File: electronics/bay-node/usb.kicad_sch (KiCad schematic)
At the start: 21 parts, among them J3 PC, J4 DUT, J7 DATA, SW3 SERVICE, U4 USBLC6-2SC6, U5 MUX_PC, U6 MUX_DUT, U7 SN74LVC1G32DBVR, U8 USBLC6-2SC6

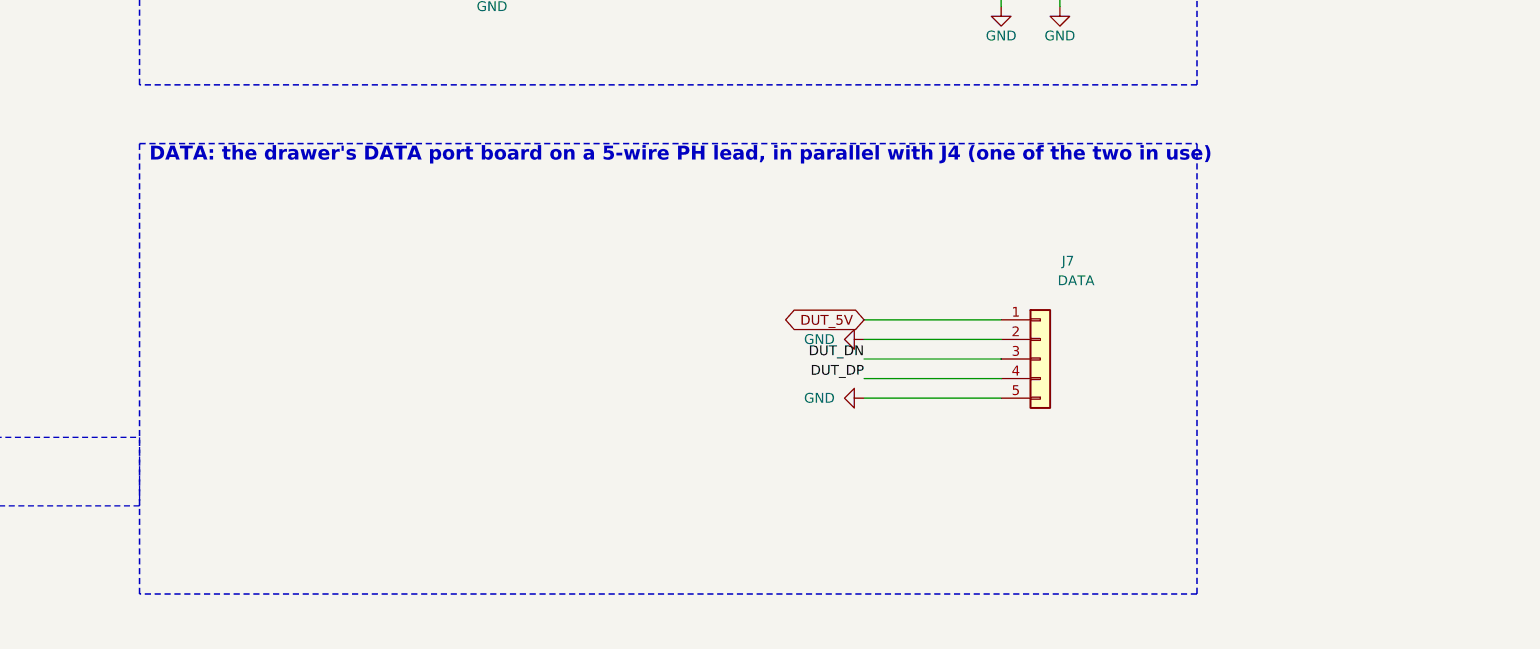
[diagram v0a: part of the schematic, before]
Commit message: DATA lead on 8 wires: node J7 a vertical PH 8 (USB, I²C, INT), data port J2 an S8B
Density decisions of 2026-10-19: the DATA lead becomes the camera's PH 8
"Same direction" type and also carries the node's I²C and an open-drain,
active-low INT (IO4, 10k pull-up, 1k at J7) for a later DATA ×4 board.

- Node: J7 B8B vertical by the right edge (J5's old slot), J5 AUX
  horizontal in the middle, AUX parts in a column between them.  J7 now
  taps the pair at J4's pads (DUT_CONN_*, behind U8's ESD like J4); the
  branch is hand-drawn in usb_hs_routes() on B.Cu under J4, since
  Freerouting found no room on U8's mux side.  ERC 0, DRC 0, parity 0,
  99 models.
- Data port: S8B, pins 1–3 open, PH at x 14.4, left hole (2.6, 13.5),
  one silkscreen label per pin.  ERC 0, DRC 0, parity 0.
- Pin map (README, check_pinmap: DATA_INT reserved), docs, cabling,
  BOM (one PH 8 lead type for DATA and camera, no B5B/S5B), SCAD config.

Co-Authored-By: Claude Opus 5.5 <noreply@anthropic.com>
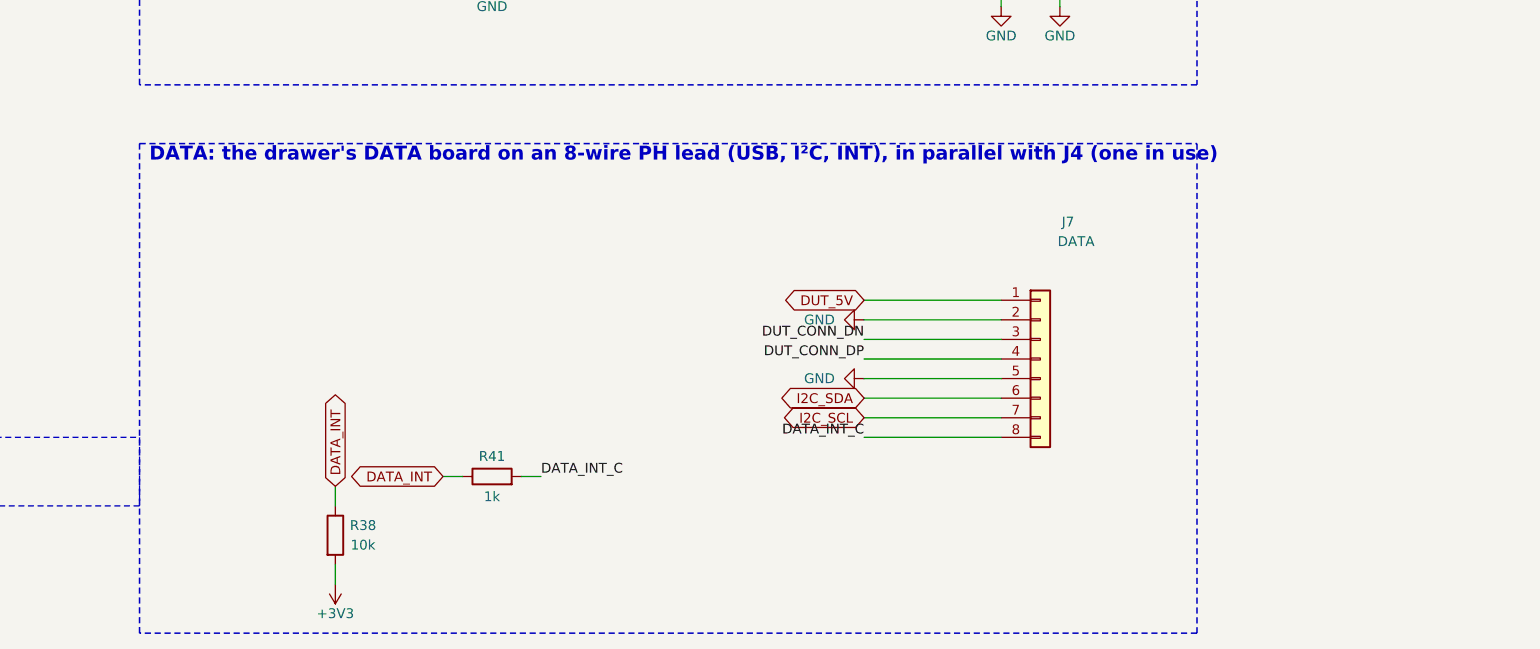
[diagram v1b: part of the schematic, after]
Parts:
- added R38: 10k, Resistor_SMD:R_0603_1608Metric, symbol Device:R
- added R41: 1k, Resistor_SMD:R_0603_1608Metric, symbol Device:R
- J7: footprint Connector_JST:JST_PH_B5B-PH-SM4-TB_1x05-1MP_P2.00mm_Vertical -> Connector_JST:JST_PH_B8B-PH-SM4-TB_1x08-1MP_P2.00mm_Vertical; symbol Connector_Generic:Conn_01x05 -> Connector_Generic:Conn_01x08; LCSC C265085 -> C495548; MPN B5B-PH-SM4-TB(LF)(SN) -> B8B-PH-SM4-TB(LF)(SN)
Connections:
- net +3V3: now also R38.2
- net DUT_CONN_DN: now also J7.3 (Pin_3)
- net DUT_CONN_DP: now also J7.4 (Pin_4)
- net DUT_DN: no longer J7.3 (Pin_3)
- net DUT_DP: no longer J7.4 (Pin_4)
- new net DATA_INT: R38.1, R41.1
- new net DATA_INT_C: J7.8 (Pin_8), R41.2
- new net I2C_SCL: J7.7 (Pin_7)
- new net I2C_SDA: J7.6 (Pin_6)
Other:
- note added: "DATA: the drawer's DATA board on an 8-wire PH lead (USB, I²C, INT), in parallel with J4 (one in use)"
- note removed: "DATA: the drawer's DATA port board on a 5-wire PH lead, in parallel with J4 (one of the two in use)"

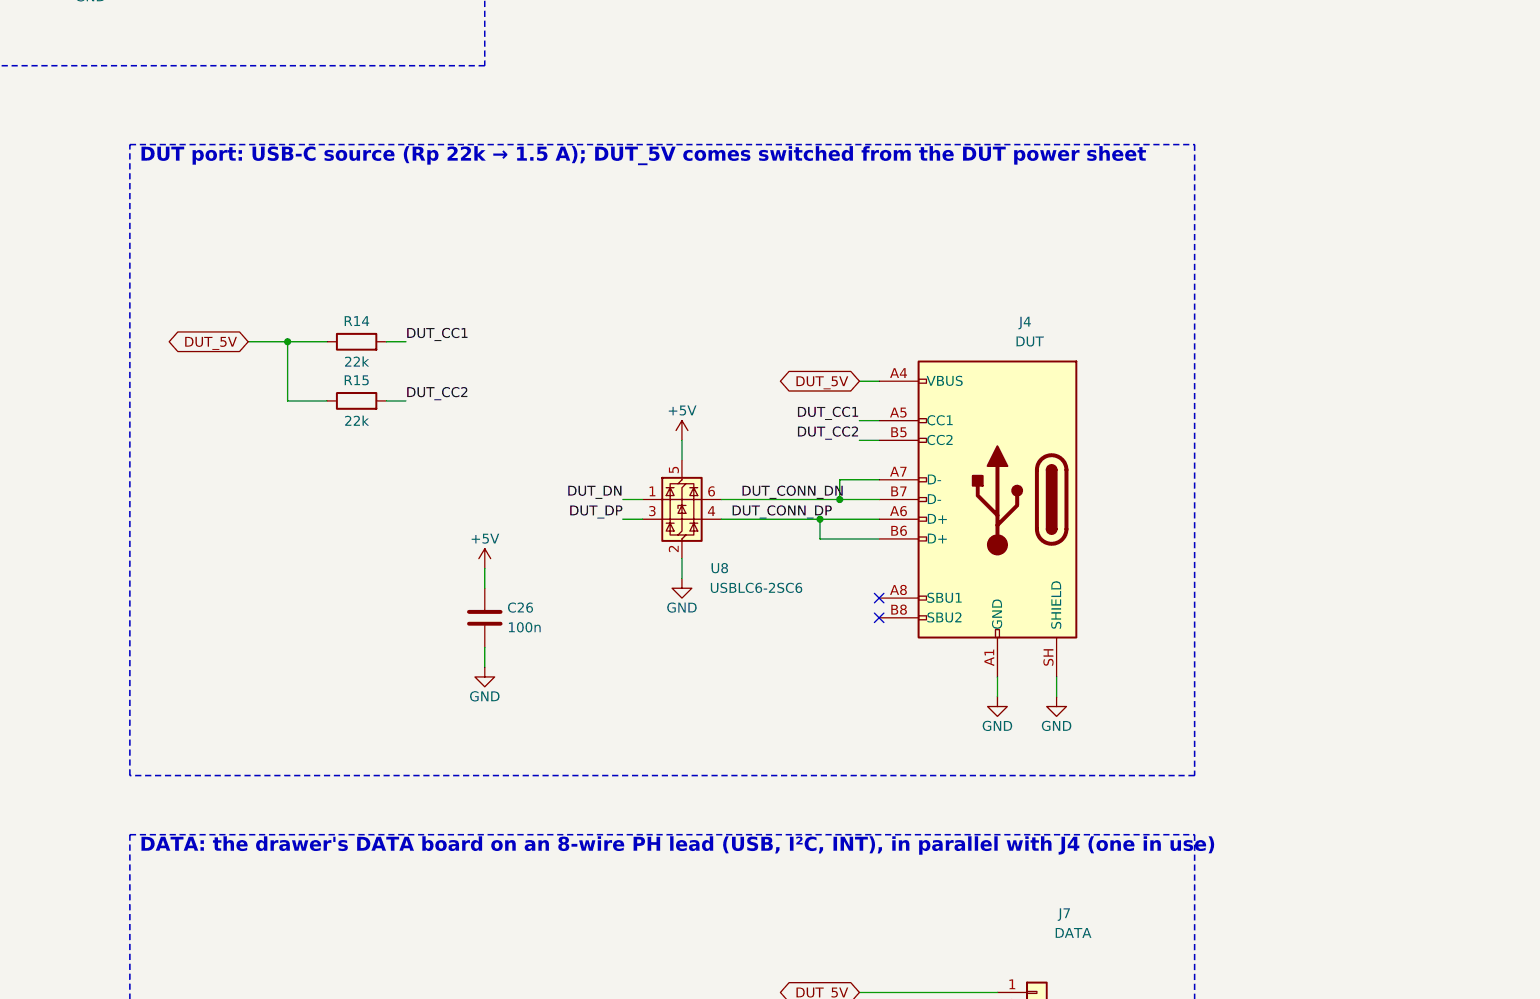
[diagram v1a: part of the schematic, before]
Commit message: Bay node 74 × 90: no J4, AUX and DATA side entry on the right edge
The node grows 10 mm on the right and drops the DUT receptacle J4 (the
user's option B, 2026-10-19): every DUT hangs on the DATA lead.

- J7 (DATA, S8B) and J5 (AUX, S6B) are side entry on the right edge,
  facing the drag chain; J6 (CAM) stays vertical at the rear right, its
  lead straight back, east of the antenna keep-out.  J2 and the right
  holes (x 70.5) move to the new edge; the front half and the left holes
  stay (the tray's access holes, a09923f).
- U8 is the last part before J7; the hand-drawn HS chain ends on J7's
  pads (DUT_CONN matched with its two vias).  R14/R15 go with J4.
- +5V at 5.24 V (FB 100k/18k) for the DATA board at 1.4 A; INA226 Vbus
  on Vin- at its pins.
- Docs: electronics, cabling, assembly, power (no batteries on rack
  DUTs), the third Konnect round; BOM and JLC estimate (≈ $328), web
  scene's DATA plug, notice NODE_DATA.

Co-Authored-By: Claude Opus 5.5 <noreply@anthropic.com>
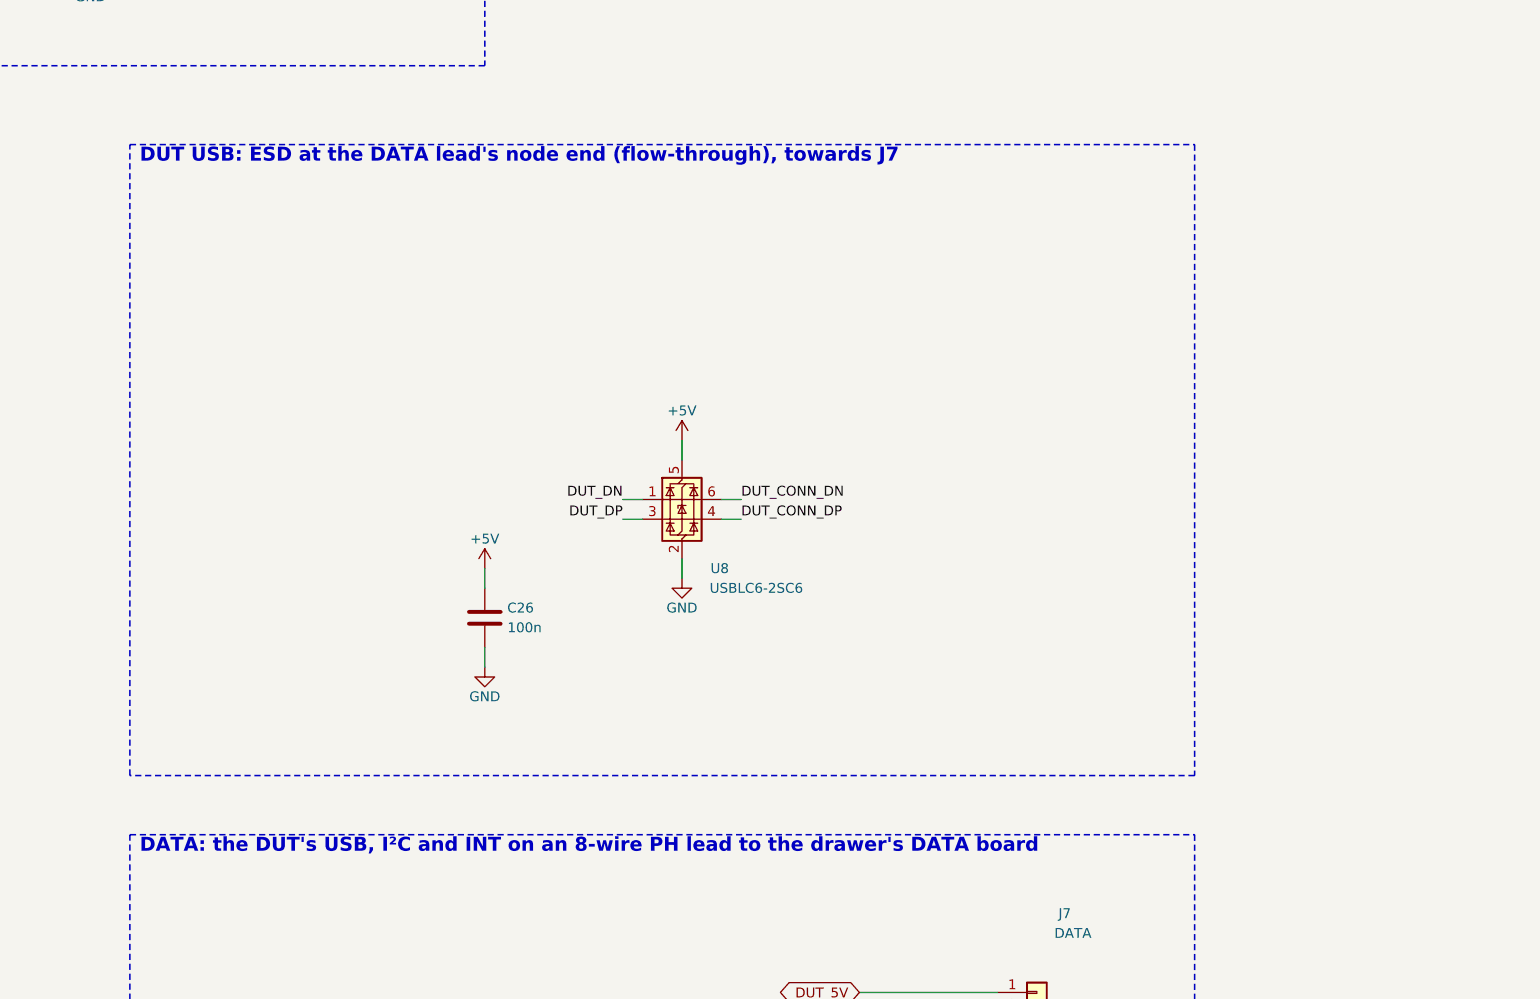
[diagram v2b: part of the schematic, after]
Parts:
- removed J4: DUT, Connector_USB:USB_C_Receptacle_GCT_USB4105-xx-A_16P_TopMnt_Horizontal, symbol Connector:USB_C_Receptacle_USB2.0_16P
- removed R14, R15: 22k, Resistor_SMD:R_0603_1608Metric, symbol Device:R
- J7: footprint Connector_JST:JST_PH_B8B-PH-SM4-TB_1x08-1MP_P2.00mm_Vertical -> Connector_JST:JST_PH_S8B-PH-SM4-TB_1x08-1MP_P2.00mm_Horizontal; LCSC C495548 -> C265121; MPN B8B-PH-SM4-TB(LF)(SN) -> S8B-PH-SM4-TB(LF)(SN)
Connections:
- no-connect marks 4 -> 2
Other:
- note added: "DATA: the DUT's USB, I²C and INT on an 8-wire PH lead to the drawer's DATA board"
- note added: "DUT USB: ESD at the DATA lead's node end (flow-through), towards J7"
- note removed: "DATA: the drawer's DATA board on an 8-wire PH lead (USB, I²C, INT), in parallel with J4 (one in use)"
- note removed: "DUT port: USB-C source (Rp 22k → 1.5 A); DUT_5V comes switched from the DUT power sheet"

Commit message: Bay node: J7 takes D+ on pin 3, the DUT pair runs straight
U8 puts D- to the north and J7's side entry put D+ there, so D+ crossed
under D- on B.Cu.  The user chose to swap J7's pins 3/4 (3 D+, 4 D-):
DUT_CONN_DP/DN now run straight from U8 into J7, one 45° step each, no
via (14.6 / 14.7 mm; J3 -> J7 matched to ≈ 0.3 mm).

The data port follows through the lead (pin n <-> 9-n): J2 5 D-, 6 D+,
and U1's channels swap with it (D+ through 1/6), so every pad keeps the
copper it had.  Both boards re-routed: ERC 0, DRC 0, 0 unconnected,
parity 0, JLC READY.

The node's buck GND and +5V islands and the LDO tab are now exclusive
(0.5 mm), as on the hub: Freerouting cut buck-5v, then C12 off the LDO
tab.  Docs: electronics (HS path, J7 and lead pinouts), cabling, the
third Konnect round; BOM note.

Co-Authored-By: Claude Opus 5.5 <noreply@anthropic.com>
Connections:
- net DUT_CONN_DN: now also J7.4 (Pin_4); no longer J7.3 (Pin_3)
- net DUT_CONN_DP: now also J7.3 (Pin_3); no longer J7.4 (Pin_4)
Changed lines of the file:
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@@
 		)
 	)
-	(label "DUT_CONN_DN"
+	(label "DUT_CONN_DP"
 		(at 363.22 215.9 180)
 		(fields_autoplaced yes)
@@
 		)
 	)
-	(label "DUT_CONN_DP"
+	(label "DUT_CONN_DN"
 		(at 363.22 218.44 180)
 		(fields_autoplaced yes)

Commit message: Hub 37 and node 38 part types: more values merged
From the JLC cost session's list (it does the analysis, this session
edits the boards).  No footprint or track moves; both boards regenerated
on their Freerouting sessions (node 996/386, hub 1241/593 segments/vias),
ERC 0, DRC 0 errors (the hub's known C8 silkscreen warning), parity 0.

- Hub: the IMON filters and the CAN split caps on the dVdT caps' 22 nF
  (IMON RC 22 µs; the split cap only filters common mode): 38 -> 37 types,
  -$17.05 of feeders against the quote, order ≈ $212.77.
- Node: buck EN 100k/10k (same 13.5 V / 10.8 V), PC_DET 10k/18k (3.2 V),
  I²C pull-ups 5.1k, AUX VREF 33 Ω: 42 -> 38 types, estimate ≈ $322.77.

Docs: electronics.md (the hub's types per block, the node's estimate),
can.md, firmware pin tables.

Co-Authored-By: Claude Opus 5.5 <noreply@anthropic.com>
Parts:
- R12: value 20k -> 18k; LCSC C4184 -> C25810; MPN 0603WAF2002T5E -> 0603WAF1802T5E
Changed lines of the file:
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@@
 			)
 		)
-		(property "Value" "20k"
+		(property "Value" "18k"
 			(at 110.271 60.96 0)
 			(effects
@@
 			)
 		)
-		(property "Description" "Resistor 20k 0603"
+		(property "Description" "Resistor 18k 0603"
 			(at 106.68 59.69 0)
 			(effects
@@
 			)
 		)
-		(property "LCSC" "C4184"
+		(property "LCSC" "C25810"
 			(at 106.68 59.69 0)
 			(effects
@@
 			)
 		)
-		(property "MPN" "0603WAF2002T5E"
+		(property "MPN" "0603WAF1802T5E"
 			(at 106.68 59.69 0)
 			(effects
